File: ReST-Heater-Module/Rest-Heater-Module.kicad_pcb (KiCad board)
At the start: 2 copper layers, 24.5 x 29.5 mm, 17 parts

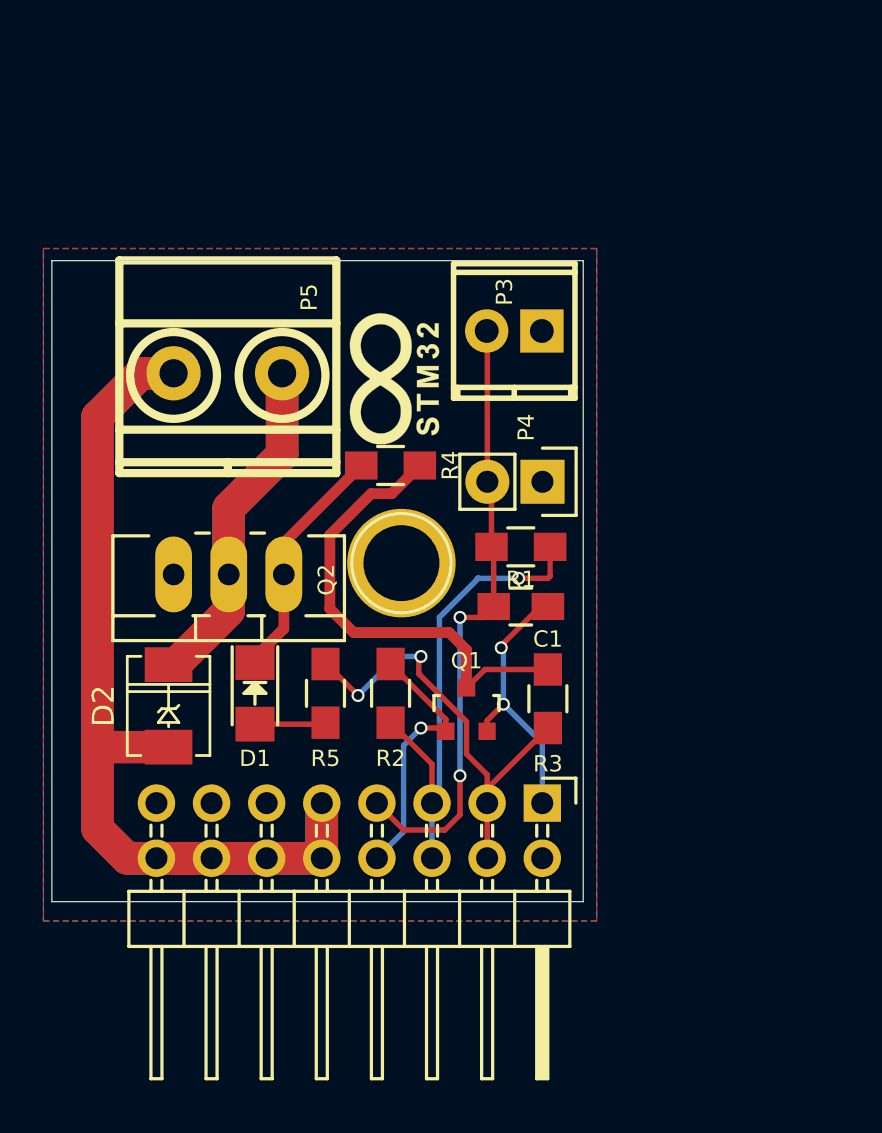
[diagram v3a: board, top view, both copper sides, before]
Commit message: Finally removed all unnecessary Libs and added Heatsink for 5V Regulator
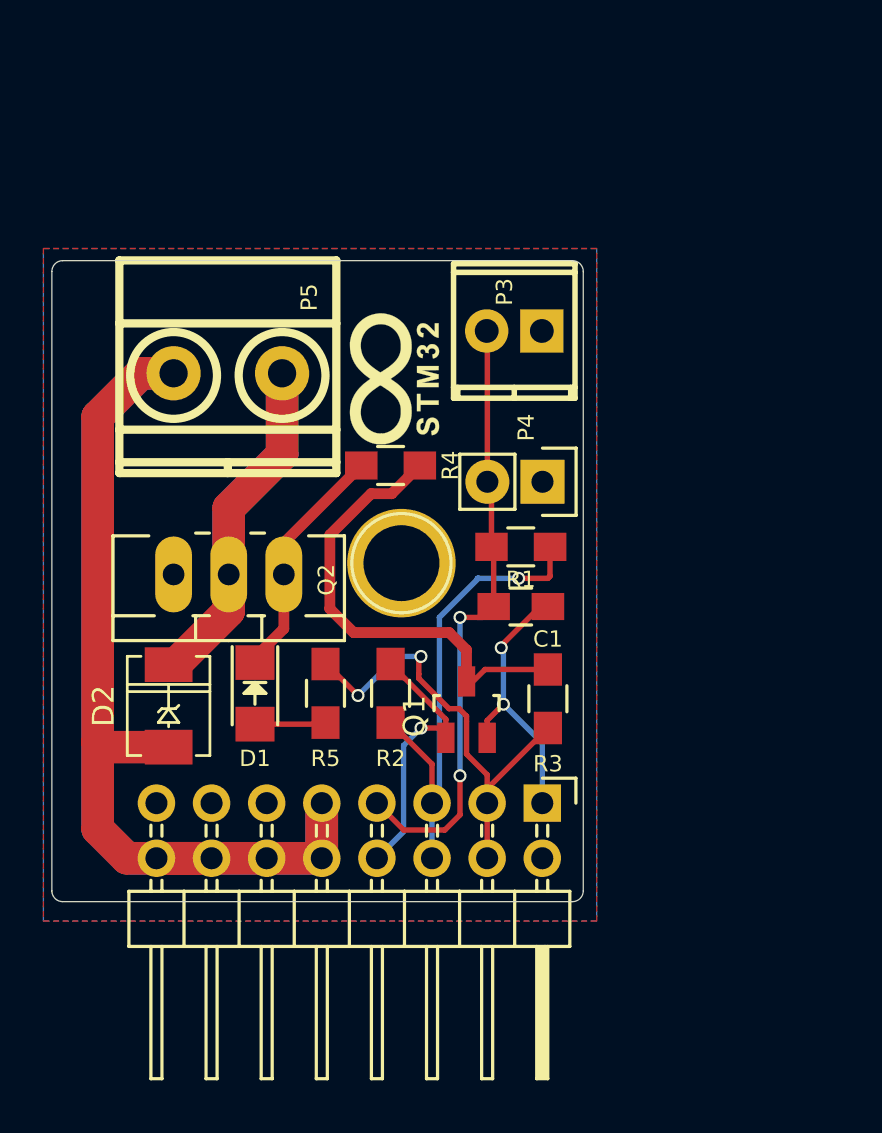
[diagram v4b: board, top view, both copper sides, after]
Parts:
- Q1: footprint TO_SOT_Packages_SMD:SOT-23 -> ReST-Library:SOT-23
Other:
- outline, holes or cut-outs redrawn
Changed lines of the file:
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@@
     (links 34)
     (no_connects 0)
-    (area 132.884999 105.054999 157.385001 134.605001)
+    (area 132.5 104.5 159.575 143.485001)
     (thickness 1.6)
-    (drawings 5)
-    (tracks 112)
+    (drawings 9)
+    (tracks 116)
     (zones 0)
     (modules 17)
@@
       (scale (xyz 1 1 1))
       (rotate (xyz 0 0 90))
-    )
-  )
-  (module TO_SOT_Packages_SMD:SOT-23 (layer F.Cu)
-    (at 152 125.75)
-    (descr "SOT-23, Standard")
-    (tags SOT-23)
-    (attr smd)
-    (fp_text reference Q1 (at 0 -2.25) (layer F.SilkS)
-      (effects (font (size 0.75 0.75) (thickness 0.1)))
-    )
-    (fp_text value "" (at 0 2.3) (layer F.Fab)
-      (effects (font (size 1 1) (thickness 0.15)))
-    )
-    (fp_line (start -1.65 -1.6) (end 1.65 -1.6) (layer F.CrtYd) (width 0.05))
-    (fp_line (start 1.65 -1.6) (end 1.65 1.6) (layer F.CrtYd) (width 0.05))
-    (fp_line (start 1.65 1.6) (end -1.65 1.6) (layer F.CrtYd) (width 0.05))
-    (fp_line (start -1.65 1.6) (end -1.65 -1.6) (layer F.CrtYd) (width 0.05))
-    (fp_line (start 1.29916 -0.65024) (end 1.2509 -0.65024) (layer F.SilkS) (width 0.15))
-    (fp_line (start -1.49982 0.0508) (end -1.49982 -0.65024) (layer F.SilkS) (width 0.15))
-    (fp_line (start -1.49982 -0.65024) (end -1.2509 -0.65024) (layer F.SilkS) (width 0.15))
-    (fp_line (start 1.29916 -0.65024) (end 1.49982 -0.65024) (layer F.SilkS) (width 0.15))
-    (fp_line (start 1.49982 -0.65024) (end 1.49982 0.0508) (layer F.SilkS) (width 0.15))
-    (pad 1 smd rect (at -0.95 1.00076) (size 0.8001 0.8001) (layers F.Cu F.Paste F.Mask)
-      (net 7 /PWM-HEATER))
-    (pad 2 smd rect (at 0.95 1.00076) (size 0.8001 0.8001) (layers F.Cu F.Paste F.Mask)
-      (net 2 GND))
-    (pad 3 smd rect (at 0 -0.99822) (size 0.8001 0.8001) (layers F.Cu F.Paste F.Mask)
-      (net 10 "Net-(Q1-Pad3)"))
-    (model TO_SOT_Packages_SMD.3dshapes/SOT-23.wrl
-      (at (xyz 0 0 0))
-      (scale (xyz 1 1 1))
-      (rotate (xyz 0 0 0))
     )
   )
@@
     (pad 1 thru_hole circle (at 0 0) (size 5 5) (drill 3.5) (layers *.Cu *.Mask F.SilkS))
   )
+  (module ReST-Library:SOT-23 (layer F.Cu)
+    (at 152 125.75)
+    (descr "SOT-23, Standard")
+    (tags SOT-23)
+    (attr smd)
+    (fp_text reference Q1 (at -2.4 0.3 90) (layer F.SilkS)
+      (effects (font (size 1 1) (thickness 0.15)))
+    )
+    (fp_text value "" (at 0 2.3) (layer F.Fab)
+      (effects (font (size 1 1) (thickness 0.15)))
+    )
+    (fp_line (start -1.65 -1.6) (end 1.65 -1.6) (layer F.CrtYd) (width 0.05))
+    (fp_line (start 1.65 -1.6) (end 1.65 1.6) (layer F.CrtYd) (width 0.05))
+    (fp_line (start 1.65 1.6) (end -1.65 1.6) (layer F.CrtYd) (width 0.05))
+    (fp_line (start -1.65 1.6) (end -1.65 -1.6) (layer F.CrtYd) (width 0.05))
+    (fp_line (start 1.29916 -0.65024) (end 1.2509 -0.65024) (layer F.SilkS) (width 0.15))
+    (fp_line (start -1.49982 0.0508) (end -1.49982 -0.65024) (layer F.SilkS) (width 0.15))
+    (fp_line (start -1.49982 -0.65024) (end -1.2509 -0.65024) (layer F.SilkS) (width 0.15))
+    (fp_line (start 1.29916 -0.65024) (end 1.49982 -0.65024) (layer F.SilkS) (width 0.15))
+    (fp_line (start 1.49982 -0.65024) (end 1.49982 0.0508) (layer F.SilkS) (width 0.15))
+    (pad 1 smd rect (at -0.95 1.3) (size 0.8001 1.4) (layers F.Cu F.Paste F.Mask)
+      (net 7 /PWM-HEATER))
+    (pad 2 smd rect (at 0.95 1.3) (size 0.8001 1.4) (layers F.Cu F.Paste F.Mask)
+      (net 2 GND))
+    (pad 3 smd rect (at 0 -1.3) (size 0.8001 1.4) (layers F.Cu F.Paste F.Mask)
+      (net 10 "Net-(Q1-Pad3)"))
+    (model TO_SOT_Packages_SMD.3dshapes/SOT-23.wrl
+      (at (xyz 0 0 0))
+      (scale (xyz 1 1 1))
+      (rotate (xyz 0 0 0))
+    )
+  )
+  (gr_arc (start 133.39 134.1) (end 133.39 134.6) (angle 90) (layer Edge.Cuts) (width 0.01))
+  (gr_arc (start 133.39 105.56) (end 132.89 105.56) (angle 90) (layer Edge.Cuts) (width 0.01))
+  (gr_arc (start 156.88 105.56) (end 156.88 105.06) (angle 90) (layer Edge.Cuts) (width 0.01))
+  (gr_arc (start 156.88 134.1) (end 157.38 134.1) (angle 90) (layer Edge.Cuts) (width 0.01))
+  (gr_line (start 133.39 134.6) (end 156.88 134.6) (angle 90) (layer Edge.Cuts) (width 0.01))
+  (gr_line (start 132.89 105.56) (end 132.89 134.1) (angle 90) (layer Edge.Cuts) (width 0.01))
+  (gr_line (start 156.88 105.06) (end 133.39 105.06) (angle 90) (layer Edge.Cuts) (width 0.01))
+  (gr_line (start 157.38 134.1) (end 157.38 105.56) (angle 90) (layer Edge.Cuts) (width 0.01))
   (gr_text "ReST32 Heater\nRev. A | Test\nPCB by Straw" (at 144.35 124.7) (layer B.SilkS)
     (effects (font (size 1.5 1.5) (thickness 0.3)) (justify mirror))
   )
-  (gr_line (start 132.89 105.06) (end 132.89 134.6) (angle 90) (layer Edge.Cuts) (width 0.01))
-  (gr_line (start 157.38 105.06) (end 132.89 105.06) (angle 90) (layer Edge.Cuts) (width 0.01))
-  (gr_line (start 157.38 134.6) (end 157.38 105.06) (angle 90) (layer Edge.Cuts) (width 0.01))
-  (gr_line (start 132.89 134.6) (end 157.38 134.6) (angle 90) (layer Edge.Cuts) (width 0.01))
   (segment (start 147.87 130.06) (end 149.11 131.3) (width 0.25) (layer F.Cu) (net 1))
   (segment (start 151.7 121.5) (end 152.75 121.5) (width 0.25) (layer F.Cu) (net 1))
@@
   (segment (start 150.75 129.72) (end 150.41 130.06) (width 0.25) (layer B.Cu) (net 8))
   (segment (start 150.41 130.06) (end 150.41 132.6) (width 0.25) (layer B.Cu) (net 8))
+  (segment (start 152 126.3) (end 152 126.05) (width 0.25) (layer F.Cu) (net 9))
+  (segment (start 152 127.8) (end 152 126.3) (width 0.25) (layer F.Cu) (net 9))
+  (segment (start 152.95 128.75) (end 152 127.8) (width 0.25) (layer F.Cu) (net 9))
+  (segment (start 152.95 130.06) (end 152.95 128.75) (width 0.25) (layer F.Cu) (net 9))
+  (segment (start 149.8 123.4) (end 149.8 124.1) (width 0.25) (layer F.Cu) (net 9))
+  (segment (start 149.9 123.3) (end 149.8 123.4) (width 0.25) (layer F.Cu) (net 9))
+  (via (at 149.9 123.3) (size 0.6) (drill 0.4) (layers F.Cu B.Cu) (net 9))
+  (segment (start 148.8 123.3) (end 149.9 123.3) (width 0.25) (layer B.Cu) (net 9))
+  (segment (start 147 125.1) (end 148.8 123.3) (width 0.25) (layer B.Cu) (net 9))
+  (via (at 147 125.1) (size 0.6) (drill 0.4) (layers F.Cu B.Cu) (net 9))
+  (segment (start 147 125.1) (end 145.55 123.65) (width 0.25) (layer F.Cu) (net 9))
+  (segment (start 149.8 124.313602) (end 149.8 124.1) (width 0.25) (layer F.Cu) (net 9))
+  (segment (start 151.193199 125.706801) (end 149.8 124.313602) (width 0.25) (layer F.Cu) (net 9))
+  (segment (start 151.656801 125.706801) (end 151.193199 125.706801) (width 0.25) (layer F.Cu) (net 9))
+  (segment (start 152 126.05) (end 151.656801 125.706801) (width 0.25) (layer F.Cu) (net 9))
   (segment (start 145.5 123.65) (end 145.55 123.65) (width 0.25) (layer F.Cu) (net 9))
-  (segment (start 145.55 123.65) (end 147 125.1) (width 0.25) (layer F.Cu) (net 9))
-  (via (at 147 125.1) (size 0.6) (drill 0.4) (layers F.Cu B.Cu) (net 9))
-  (segment (start 147 125.1) (end 148.8 123.3) (width 0.25) (layer B.Cu) (net 9))
-  (segment (start 148.8 123.3) (end 149.9 123.3) (width 0.25) (layer B.Cu) (net 9))
-  (via (at 149.9 123.3) (size 0.6) (drill 0.4) (layers F.Cu B.Cu) (net 9))
-  (segment (start 149.9 123.3) (end 149.8 123.4) (width 0.25) (layer F.Cu) (net 9))
-  (segment (start 149.8 123.4) (end 149.8 124.1) (width 0.25) (layer F.Cu) (net 9))
-  (segment (start 152.95 130.06) (end 152.95 128.75) (width 0.25) (layer F.Cu) (net 9))
-  (segment (start 152.95 128.75) (end 152 127.8) (width 0.25) (layer F.Cu) (net 9))
-  (segment (start 152 127.8) (end 152 126.3) (width 0.25) (layer F.Cu) (net 9))
-  (segment (start 152 126.3) (end 149.8 124.1) (width 0.25) (layer F.Cu) (net 9))
   (segment (start 152.95 130.06) (end 152.95 129.4) (width 0.25) (layer F.Cu) (net 9))
   (segment (start 152.95 129.4) (end 155.75 126.6) (width 0.25) (layer F.Cu) (net 9))
